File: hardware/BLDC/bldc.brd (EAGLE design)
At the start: 51 x 40 mm, 84 parts, among them J1 PWR_2_XT30PW-M, J2 LINEAR_3_JST_PH_RA, J3 LINEAR_8_JST_PH_RA, U1 MA702, U10 MCP2542FD, U11 LDFM33PUR, U2 DRV8323RS, U3 TPN7R006PL, U4 TPN7R006PL, U5 TPN7R006PL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

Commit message: Oops, no longer grounded INLx
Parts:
- C14: value 2.2uF 50V -> 10uF 50V
- R12: value 5 -> 22
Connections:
- net DRV_ENABLE: now also U2.38, U2.40, U2.42
- net GND: no longer U2.38, U2.40, U2.42
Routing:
- net DRV_ENABLE: track 26.9 -> 37.7 mm, vias 2 -> 3
- net GND: track 66.4 -> 63.0 mm
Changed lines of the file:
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@@
 </layers>
 <board>
-<fusionsync huburn="a.YnVzaW5lc3M6Z21haWwyMjE5MTc" projecturn="a.YnVzaW5lc3M6Z21haWwyMjE5MTcjMjAxOTA2MjkyMDE0MTU5NzY" f3durn="urn:adsk.wipprod:dm.lineage:e4urj2y-ReajaBtUk_DaUw" pcbguid="" lastpulledtime="" lastsyncedchangeguid="" latestrevisionid="0cfa6979-0abf-47e5-904f-7e41c382e9f9" lastsyncedrevisionid="0cfa6979-0abf-47e5-904f-7e41c382e9f9" lastboardhashguid="129d7aed-9189-2586-7fe0-9e496c46e9fb" lastpushedtime="2020-05-19T04:37:09Z" linktopcb3d="%12"/>
 <plain>
 <wire x1="39.0836" y1="39.681" x2="38" y2="40" width="0" layer="20" curve="32.8049"/>
@@
 <attribute name="VALUE" x="9.24" y="26.43" size="1.27" layer="27" rot="R90"/>
 </element>
-<element name="C14" library="_T_rcl" library_urn="urn:adsk.eagle:library:19571919" package="C0603" package3d_urn="urn:adsk.eagle:package:19572011/3" value="2.2uF 50V" x="3.2" y="33.2" smashed="yes" rot="R270">
+<element name="C14" library="_T_rcl" library_urn="urn:adsk.eagle:library:19571919" package="C0603" package3d_urn="urn:adsk.eagle:package:19572011/3" value="10uF 50V" x="3.2" y="33.2" smashed="yes" rot="R270">
 <attribute name="NAME" x="4.47" y="34.47" size="1.27" layer="25" rot="R270"/>
 <attribute name="VALUE" x="0.66" y="34.47" size="1.27" layer="27" rot="R270"/>
@@
 <attribute name="VALUE" x="46.53" y="25.66" size="1.27" layer="27"/>
 </element>
-<element name="R12" library="_T_rcl" library_urn="urn:adsk.eagle:library:19571919" package="R0402" package3d_urn="urn:adsk.eagle:package:19572014/3" value="5" x="45.3" y="25.6" smashed="yes" rot="R180">
+<element name="R12" library="_T_rcl" library_urn="urn:adsk.eagle:library:19571919" package="R0402" package3d_urn="urn:adsk.eagle:package:19572014/3" value="22" x="45.3" y="25.6" smashed="yes" rot="R180">
 <attribute name="NAME" x="46.57" y="24.33" size="1.27" layer="25" rot="R180"/>
 <attribute name="VALUE" x="46.57" y="28.14" size="1.27" layer="27" rot="R180"/>
@@
 <wire x1="30.5544" y1="31.35" x2="31.05" y2="31.35" width="0.2" layer="1"/>
 <wire x1="31.05" y1="31.35" x2="31.7" y2="32" width="0.2" layer="1"/>
-<wire x1="30.47019375" y1="36.3452" x2="29.76779375" y2="37.0476" width="0.2" layer="1"/>
-<wire x1="31.7" y1="35.345975" x2="30.700775" y2="36.3452" width="0.2" layer="1"/>
-<wire x1="30.700775" y1="36.3452" x2="30.47019375" y2="36.3452" width="0.2" layer="1"/>
+<wire x1="31.7" y1="35.11539375" x2="29.76779375" y2="37.0476" width="0.2" layer="1"/>
 <wire x1="13" y1="36.3" x2="13" y2="34.925" width="0.2" layer="1"/>
-<wire x1="31.7" y1="32" x2="31.7" y2="35.345975" width="0.2" layer="1"/>
+<wire x1="31.7" y1="32" x2="31.7" y2="35.11539375" width="0.2" layer="1"/>
 <wire x1="29.76779375" y1="37.0476" x2="13.7476" y2="37.0476" width="0.2" layer="1"/>
 <wire x1="13.7476" y1="37.0476" x2="13" y2="36.3" width="0.2" layer="1"/>
@@
 <contactref element="U2" pad="31"/>
 <via x="19.4" y="25.4" extent="1-16" drill="0.3"/>
-<wire x1="15.86168125" y1="25.66168125" x2="16.7" y2="26.5" width="0.2" layer="1"/>
-<wire x1="18.3" y1="26.5" x2="16.7" y2="26.5" width="0.2" layer="1"/>
+<wire x1="14.807384375" y1="24.6309375" x2="16.676446875" y2="26.5" width="0.2" layer="1"/>
+<wire x1="18.3" y1="26.5" x2="16.676446875" y2="26.5" width="0.2" layer="1"/>
 <wire x1="18.3" y1="26.5" x2="19.4" y2="25.4" width="0.2" layer="1"/>
 <wire x1="19.4" y1="25.4" x2="30.5952" y2="25.4" width="0.2" layer="16"/>
@@
 <wire x1="31.6" y1="26.4048" x2="31.5452" y2="26.35" width="0.2" layer="1"/>
 <wire x1="31.5452" y1="26.35" x2="30.5544" y2="26.35" width="0.2" layer="1"/>
-<wire x1="14.807384375" y1="24.6309375" x2="15.838128125" y2="25.66168125" width="0.2" layer="1"/>
-<wire x1="15.838128125" y1="25.66168125" x2="15.86168125" y2="25.66168125" width="0.2" layer="1"/>
 </signal>
 <signal name="DRV_CS">
@@
 <contactref element="J3" pad="3"/>
 <wire x1="29.85" y1="32.65" x2="29.85" y2="32.0544" width="0.2" layer="1"/>
-<wire x1="31.3476" y1="35.2" x2="31.3476" y2="34.1476" width="0.2" layer="1"/>
+<wire x1="31.3476" y1="34.96941875" x2="31.3476" y2="34.1476" width="0.2" layer="1"/>
 <wire x1="31.3476" y1="34.1476" x2="29.85" y2="32.65" width="0.2" layer="1"/>
 <wire x1="14" y1="34.925" x2="14" y2="36.1952" width="0.2" layer="1"/>
 <wire x1="14" y1="36.1952" x2="14.5" y2="36.6952" width="0.2" layer="1"/>
 <wire x1="14.5" y1="36.6952" x2="29.62181875" y2="36.6952" width="0.2" layer="1"/>
-<wire x1="30.32421875" y1="35.9928" x2="30.5548" y2="35.9928" width="0.2" layer="1"/>
-<wire x1="30.5548" y1="35.9928" x2="31.3476" y2="35.2" width="0.2" layer="1"/>
-<wire x1="29.62181875" y1="36.6952" x2="30.32421875" y2="35.9928" width="0.2" layer="1"/>
+<wire x1="29.62181875" y1="36.6952" x2="31.3476" y2="34.96941875" width="0.2" layer="1"/>
 </signal>
 <signal name="SWO">
@@
 <contactref element="C10" pad="2"/>
 <contactref element="C11" pad="2"/>
-<contactref element="U2" pad="38"/>
-<contactref element="U2" pad="42"/>
-<contactref element="U2" pad="40"/>
 <contactref element="U2" pad="43"/>
 <contactref element="C12" pad="2"/>
@@
 <wire x1="9.999059375" y1="24.277384375" x2="10.87644375" y2="23.4" width="0.2" layer="1"/>
 <wire x1="10.87644375" y1="23.4" x2="11.1" y2="23.4" width="0.2" layer="1"/>
-<wire x1="10.3526125" y1="24.6309375" x2="11.1" y2="23.88355" width="0.2" layer="1"/>
 <wire x1="11.1" y1="23.88355" x2="11.1" y2="23.4" width="0.2" layer="1"/>
-<wire x1="11.05971875" y1="25.33804375" x2="11.8977625" y2="24.5" width="0.2" layer="1"/>
 <wire x1="12.3" y1="24.5" x2="12.6" y2="24.8" width="0.2" layer="1"/>
 <wire x1="11.8977625" y1="24.5" x2="12.3" y2="24.5" width="0.2" layer="1"/>
-<wire x1="11.766825" y1="26.045153125" x2="12.6" y2="25.211978125" width="0.2" layer="1"/>
 <wire x1="12.6" y1="25.211978125" x2="12.6" y2="24.8" width="0.2" layer="1"/>
 <wire x1="16.221596875" y1="23.216725" x2="15.5" y2="22.495128125" width="0.2" layer="1"/>
@@
 <vertex x="47.2" y="11.2"/>
 <vertex x="47.2" y="20"/>
-<vertex x="49.9" y="20"/>
-<vertex x="49.9" y="-0.6"/>
+<vertex x="51.8" y="20"/>
+<vertex x="51.8" y="-0.6"/>
 <vertex x="36.1" y="-0.6"/>
 </polygon>
@@
 <wire x1="17.9" y1="26.5" x2="19.5096" y2="28.1096" width="0.2" layer="16"/>
 <wire x1="19.5096" y1="28.1096" x2="35.1" y2="28.1096" width="0.2" layer="16"/>
+<contactref element="U2" pad="38"/>
+<contactref element="U2" pad="42"/>
+<contactref element="U2" pad="40"/>
+<wire x1="11.766825" y1="26.045153125" x2="11.962653125" y2="25.849325" width="0.2" layer="1"/>
+<wire x1="11.962653125" y1="25.849325" x2="11.962653125" y2="25.431203125" width="0.2" layer="1"/>
+<wire x1="10.966559375" y1="24.435109375" x2="10.548440625" y2="24.435109375" width="0.2" layer="1"/>
+<wire x1="10.548440625" y1="24.435109375" x2="10.3526125" y2="24.6309375" width="0.2" layer="1"/>
+<wire x1="11.962653125" y1="25.431203125" x2="11.515725" y2="24.984275" width="0.2" layer="1"/>
+<wire x1="11.515725" y1="24.984275" x2="10.966559375" y2="24.435109375" width="0.2" layer="1"/>
+<wire x1="11.05971875" y1="25.33804375" x2="11.4134875" y2="24.984275" width="0.2" layer="1"/>
+<wire x1="11.4134875" y1="24.984275" x2="11.515725" y2="24.984275" width="0.2" layer="1"/>
+<wire x1="10.3526125" y1="24.6309375" x2="9.88355" y2="25.1" width="0.2" layer="1"/>
+<wire x1="9.88355" y1="25.1" x2="9.6" y2="25.1" width="0.2" layer="1"/>
+<via x="9.6" y="25.1" extent="1-16" drill="0.35"/>
+<wire x1="9.6" y1="25.1" x2="10.5" y2="26" width="0.2" layer="16"/>
+<wire x1="10.5" y1="26" x2="14" y2="26" width="0.2" layer="16"/>
+<wire x1="14" y1="26" x2="14.5" y2="26.5" width="0.2" layer="16"/>
+<wire x1="14.5" y1="26.5" x2="15.5" y2="26.5" width="0.2" layer="16"/>
 </signal>
 <signal name="SHA">
@@
 <wire x1="9.5" y1="17" x2="9.5" y2="16.6" width="0.2" layer="16"/>
 <wire x1="9.5" y1="16.6" x2="8.3" y2="15.4" width="0.2" layer="16"/>
-<wire x1="8.3" y1="15.4" x2="1.9" y2="15.4" width="0.2" layer="16"/>
-<wire x1="1.9" y1="15.4" x2="1.7" y2="15.6" width="0.2" layer="16"/>
+<wire x1="8.3" y1="15.4" x2="1.7" y2="15.4" width="0.2" layer="16"/>
+<wire x1="1.7" y1="15.4" x2="1.7" y2="15.6" width="0.2" layer="16"/>
 <via x="1.7" y="15.6" extent="1-16" drill="0.35"/>
 <wire x1="1.7" y1="15.6" x2="1.7" y2="14.62628125" width="0.2" layer="1"/>
@@
 <wire x1="14.100278125" y1="18.761953125" x2="14.82006875" y2="18.0421625" width="0.2" layer="1"/>
 <wire x1="14.82006875" y1="18.0421625" x2="16.05500625" y2="18.0421625" width="0.2" layer="1"/>
-<wire x1="20.3" y1="13.79716875" x2="20.3" y2="7.4" width="0.2" layer="1"/>
-<wire x1="20.3" y1="7.4" x2="19.3" y2="6.4" width="0.2" layer="1"/>
-<wire x1="19.3" y1="6.4" x2="18.9" y2="6.4" width="0.2" layer="1"/>
+<wire x1="20.3" y1="13.79716875" x2="20.3" y2="7.6" width="0.2" layer="1"/>
+<wire x1="20.3" y1="7.6" x2="19.1" y2="6.4" width="0.2" layer="1"/>
+<wire x1="19.1" y1="6.4" x2="18.9" y2="6.4" width="0.2" layer="1"/>
 <wire x1="16.05500625" y1="18.0421625" x2="20.3" y2="13.79716875" width="0.2" layer="1"/>
 </signal>
@@
 <wire x1="30.8" y1="7.3" x2="31.475" y2="7.3" width="0.2" layer="1"/>
 <wire x1="31.475" y1="7.3" x2="31.525" y2="7.35" width="0.2" layer="1"/>
-<wire x1="29.7048" y1="14.89195" x2="29.7048" y2="9.00805" width="0.2" layer="1"/>
-<wire x1="29.7048" y1="9.00805" x2="30" y2="8.71285" width="0.2" layer="1"/>
-<wire x1="30" y1="8.71285" x2="30" y2="8.1" width="0.2" layer="1"/>
+<wire x1="29.7048" y1="14.89195" x2="29.7048" y2="8.70805" width="0.2" layer="1"/>
+<wire x1="29.7048" y1="8.70805" x2="30" y2="8.41285" width="0.2" layer="1"/>
+<wire x1="30" y1="8.41285" x2="30" y2="8.1" width="0.2" layer="1"/>
 </signal>
 <signal name="SPA">
@@
 </note>
 <note version="8.3" severity="warning">
-Since Version 8.3, EAGLE supports Fusion synchronisation.
-This feature will not be available in this version and saving
-the document will break the link to the Fusion PCB feature.
-</note>
-<note version="8.3" severity="warning">

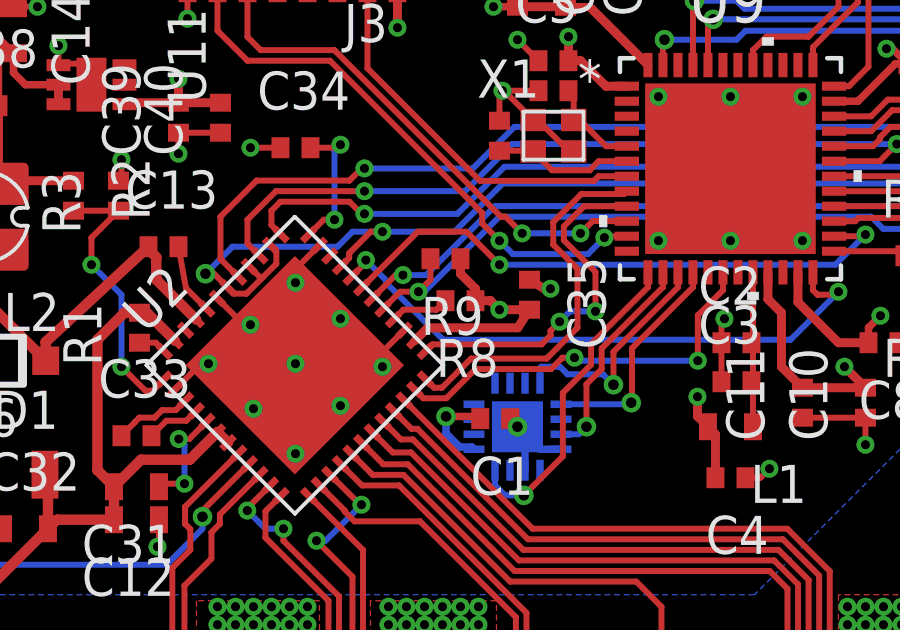
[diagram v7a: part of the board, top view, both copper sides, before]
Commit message: Fixes prior to reworking SPI2>SPI3
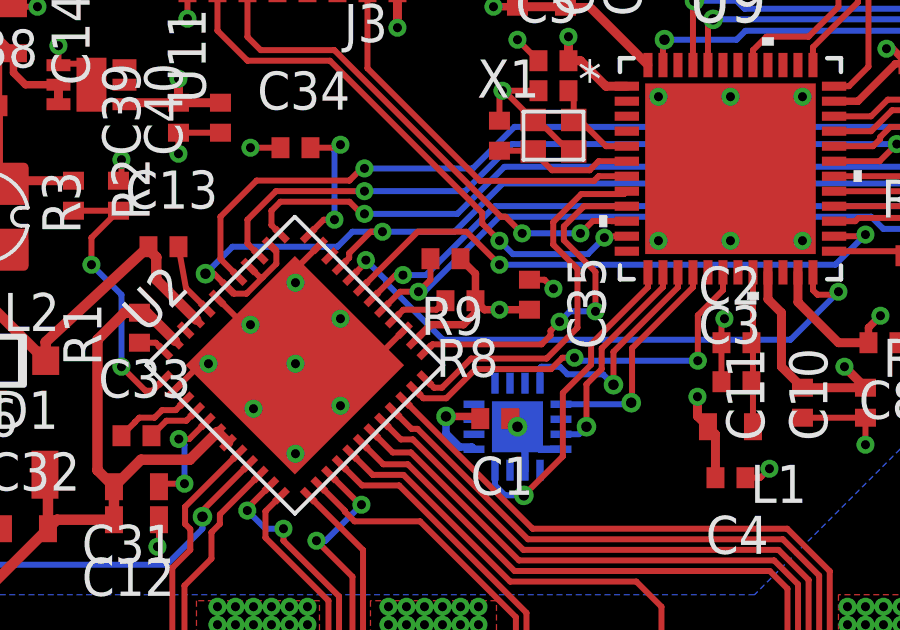
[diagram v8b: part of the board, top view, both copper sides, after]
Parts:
- R13: value 65 -> 270
- R14: value 5 -> 22
- R2: value 100k -> 54.9k 1%
- R3: value 100k -> 10k 1%
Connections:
- net VBUS_SENSE renamed VBAT_SENSE
- removed net CAL: U2.34
- net GND: now also U9.46
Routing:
- net GND: track 63.0 -> 64.6 mm, vias 123 -> 122
- net +3V3: track 47.3 -> 45.8 mm
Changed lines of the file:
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@@
 <attribute name="VALUE" x="4.74" y="30.81" size="1.27" layer="27" rot="R180"/>
 </element>
-<element name="R2" library="_T_rcl" library_urn="urn:adsk.eagle:library:19571919" package="R0402" package3d_urn="urn:adsk.eagle:package:19572014/3" value="100k" x="5.2" y="27.7" smashed="yes" rot="R270">
+<element name="R2" library="_T_rcl" library_urn="urn:adsk.eagle:library:19571919" package="R0402" package3d_urn="urn:adsk.eagle:package:19572014/3" value="54.9k 1%" x="5.2" y="27.7" smashed="yes" rot="R270">
 <attribute name="NAME" x="6.47" y="28.97" size="1.27" layer="25" rot="R270"/>
 <attribute name="VALUE" x="2.66" y="28.97" size="1.27" layer="27" rot="R270"/>
 </element>
-<element name="R3" library="_T_rcl" library_urn="urn:adsk.eagle:library:19571919" package="R0402" package3d_urn="urn:adsk.eagle:package:19572014/3" value="100k" x="6.7" y="27.7" smashed="yes" rot="R90">
+<element name="R3" library="_T_rcl" library_urn="urn:adsk.eagle:library:19571919" package="R0402" package3d_urn="urn:adsk.eagle:package:19572014/3" value="10k 1%" x="6.7" y="27.7" smashed="yes" rot="R90">
 <attribute name="NAME" x="5.43" y="26.43" size="1.27" layer="25" rot="R90"/>
 <attribute name="VALUE" x="9.24" y="26.43" size="1.27" layer="27" rot="R90"/>
@@
 <attribute name="VALUE" x="46.57" y="28.14" size="1.27" layer="27" rot="R180"/>
 </element>
-<element name="R13" library="_T_rcl" library_urn="urn:adsk.eagle:library:19571919" package="R0402" package3d_urn="urn:adsk.eagle:package:19572014/3" value="65" x="45.3" y="26.9" smashed="yes" rot="R180">
+<element name="R13" library="_T_rcl" library_urn="urn:adsk.eagle:library:19571919" package="R0402" package3d_urn="urn:adsk.eagle:package:19572014/3" value="270" x="45.3" y="26.9" smashed="yes" rot="R180">
 <attribute name="NAME" x="46.57" y="25.63" size="1.27" layer="25" rot="R180"/>
 <attribute name="VALUE" x="46.57" y="29.44" size="1.27" layer="27" rot="R180"/>
 </element>
-<element name="R14" library="_T_rcl" library_urn="urn:adsk.eagle:library:19571919" package="R0402" package3d_urn="urn:adsk.eagle:package:19572014/3" value="5" x="45.3" y="28.2" smashed="yes" rot="R180">
+<element name="R14" library="_T_rcl" library_urn="urn:adsk.eagle:library:19571919" package="R0402" package3d_urn="urn:adsk.eagle:package:19572014/3" value="22" x="45.3" y="28.2" smashed="yes" rot="R180">
 <attribute name="NAME" x="46.57" y="26.93" size="1.27" layer="25" rot="R180"/>
 <attribute name="VALUE" x="46.57" y="30.74" size="1.27" layer="27" rot="R180"/>
@@
 <contactref element="C11" pad="1"/>
 <contactref element="C10" pad="1"/>
-<contactref element="C35" pad="1"/>
 <contactref element="R8" pad="2"/>
 <contactref element="R9" pad="2"/>
@@
 <wire x1="8.7" y1="30.8" x2="8.7" y2="31.6" width="0.3" layer="1"/>
 <via x="8.7" y="31.6" extent="1-16" drill="0.3"/>
-<wire x1="18.1" y1="25.6" x2="18.1" y2="25.1" width="0.3" layer="1"/>
-<wire x1="18.6" y1="24.6" x2="18.6" y2="24.2" width="0.3" layer="1"/>
-<wire x1="18.6" y1="24.6" x2="18.1" y2="25.1" width="0.3" layer="1"/>
-<wire x1="19.1" y1="24.2" x2="18.6" y2="24.2" width="0.3" layer="1"/>
-<wire x1="19.1" y1="24.2" x2="19.4" y2="23.9" width="0.3" layer="1"/>
 <via x="19.4" y="23.9" extent="1-16" drill="0.3"/>
-<wire x1="16.575153125" y1="22.863171875" x2="17.00958125" y2="23.2976" width="0.3" layer="1"/>
-<wire x1="20.01200625" y1="23.2976" x2="20.4" y2="23.9" width="0.3" layer="1"/>
-<wire x1="17.00958125" y1="23.2976" x2="20.01200625" y2="23.2976" width="0.3" layer="1"/>
 <wire x1="16" y1="34.925" x2="16" y2="33.3" width="0.3" layer="1"/>
 <via x="16" y="33.3" extent="1-16" drill="0.3"/>
@@
 <wire x1="17.61835625" y1="20.3424" x2="18.6876" y2="20.3424" width="0.25" layer="1"/>
 <wire x1="18.6876" y1="20.3424" x2="18.76" y2="20.27" width="0.25" layer="1"/>
-<wire x1="20.4" y1="23.9" x2="19.4" y2="23.9" width="0.3" layer="1"/>
+<contactref element="C35" pad="1"/>
+<wire x1="16.575153125" y1="22.863171875" x2="17.11198125" y2="23.4" width="0.25" layer="1"/>
+<wire x1="17.11198125" y1="23.4" x2="18.2" y2="23.4" width="0.25" layer="1"/>
+<wire x1="18.2" y1="23.4" x2="18.6" y2="23.8" width="0.25" layer="1"/>
+<wire x1="18.6" y1="23.8" x2="18.6" y2="24.2" width="0.25" layer="1"/>
+<wire x1="18.6" y1="24.2" x2="18.9" y2="23.9" width="0.25" layer="1"/>
+<wire x1="18.9" y1="23.9" x2="19.4" y2="23.9" width="0.25" layer="1"/>
+<wire x1="19.4" y1="23.9" x2="20.4" y2="23.9" width="0.25" layer="1"/>
+<wire x1="18.1" y1="25.6" x2="18.6" y2="25.1" width="0.25" layer="1"/>
+<wire x1="18.6" y1="25.1" x2="18.6" y2="24.2" width="0.25" layer="1"/>
 </signal>
 <signal name="N$1">
@@
 <contactref element="U2" pad="35"/>
 <contactref element="C34" pad="2"/>
-<contactref element="C35" pad="2"/>
-<contactref element="U2" pad="27"/>
 <contactref element="R7" pad="2B"/>
 <contactref element="R7" pad="2A"/>
@@
 <via x="12.6" y="24.8" extent="1-16" drill="0.3"/>
 <via x="14.1" y="23.6" extent="1-16" drill="0.3"/>
-<via x="15.5" y="22" extent="1-16" drill="0.3"/>
 <via x="14.1" y="20.7" extent="1-16" drill="0.3"/>
 <via x="12.6" y="22.1" extent="1-16" drill="0.3"/>
@@
 <wire x1="8.05" y1="16.05" x2="8" y2="16" width="0.2" layer="1"/>
 <via x="8" y="16" extent="1-16" drill="0.3"/>
-<wire x1="20.4" y1="24.9" x2="20.8875" y2="24.6" width="0.3" layer="1"/>
-<wire x1="20.8875" y1="24.6" x2="21.1" y2="24.6" width="0.2" layer="1"/>
-<via x="21.1" y="24.6" extent="1-16" drill="0.3"/>
 <wire x1="5.8" y1="31.4" x2="5.7" y2="31.5" width="0.2" layer="1"/>
 <wire x1="5.7" y1="31.5" x2="5.7" y2="32.1" width="0.2" layer="1"/>
@@
 <wire x1="11.8977625" y1="24.5" x2="12.3" y2="24.5" width="0.2" layer="1"/>
 <wire x1="12.6" y1="25.211978125" x2="12.6" y2="24.8" width="0.2" layer="1"/>
-<wire x1="16.221596875" y1="23.216725" x2="15.5" y2="22.495128125" width="0.2" layer="1"/>
-<wire x1="15.5" y1="22.495128125" x2="15.5" y2="22" width="0.2" layer="1"/>
 <wire x1="8.58484375" y1="21.236825" x2="9.44801875" y2="22.1" width="0.2" layer="1"/>
 <wire x1="9.44801875" y1="22.1" x2="9.7" y2="22.1" width="0.2" layer="1"/>
@@
 <wire x1="21.45" y1="19.25" x2="20.75" y2="19.25" width="0.25" layer="16"/>
 <wire x1="20.75" y1="19.25" x2="20" y2="20" width="0.25" layer="16"/>
+<contactref element="U2" pad="27"/>
+<contactref element="C35" pad="2"/>
+<contactref element="U9" pad="46"/>
+<wire x1="20.4" y1="24.9" x2="20.9" y2="24.9" width="0.2" layer="1"/>
+<wire x1="20.9" y1="24.9" x2="21.2" y2="24.6" width="0.2" layer="1"/>
+<via x="21.2" y="24.6" extent="1-16" drill="0.3"/>
+<wire x1="16.221596875" y1="23.216725" x2="15.404871875" y2="22.4" width="0.2" layer="1"/>
+<wire x1="15.404871875" y1="22.4" x2="15.3" y2="22.4" width="0.2" layer="1"/>
+<wire x1="15.3" y1="22.4" x2="14.1" y2="23.6" width="0.2" layer="1"/>
+<wire x1="24.7" y1="31" x2="25.35" y2="32.0544" width="0" layer="19" extent="1-1"/>
 </signal>
 <signal name="+24V" class="2">
@@
 <wire x1="16.197765625" y1="23.9" x2="15.86804375" y2="23.570278125" width="0.2" layer="1"/>
 </signal>
-<signal name="CAL">
-<contactref element="U2" pad="34"/>
-</signal>
 <signal name="SENSE_A">
 <contactref element="U2" pad="25"/>
@@
 <wire x1="18.7523625" y1="28.1952" x2="15" y2="31.9475625" width="0.2" layer="1"/>
 </signal>
-<signal name="VBUS_SENSE">
+<signal name="VBAT_SENSE">
 <contactref element="U9" pad="25"/>
 <contactref element="R11" pad="2"/>
